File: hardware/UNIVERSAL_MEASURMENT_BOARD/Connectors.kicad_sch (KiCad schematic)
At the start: 17 parts, among them J1 2604-1104, J10 2604-1104, J11 2604-1104, J12 2604-1104, J13 2604-1104, J14 2604-1104, J15 2604-1104, J16 2604-1104, J17 2604-1104, J2 2604-1104, J3 2604-1104, J4 2604-1104, J5 2604-1104, J6 2604-1104, J7 2604-1104, J8 2604-1104, J9 2604-1104

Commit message: continued
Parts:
- removed J11, J12, J16, J3: 2604-1104, 26041104, symbol 2604-1104:2604-1104
- added D1, D10, D11, D12, D13, D14, D15, D16, D17, D18, D19, D2, D20, D21, D22, D23, D24, D25, D26, D27, D28, D29, D3, D30, D31, D32, D33, D34, D35, D36, D37, D38, D39, D4, D40, D5, D6, D7, D8, D9: TVS, symbol Device:D_TVS_Small
- added F1, F10, F11, F12, F14, F15, F16, F17, F18, F19, F2, F20, F21, F22, F23, F24, F25, F26, F27, F28, F29, F3, F30, F31, F32, F33, F34, F35, F36, F37, F4, F5, F6, F7, F8, F9: 100mA, symbol Device:Fuse_Small
- added F13: -A, symbol Device:Fuse_Small
- added unit 3 of J1
- added unit 4 of J1
- added unit 2 of J1
- added unit 2 of J10
- added unit 3 of J10
- added unit 4 of J10
- added J11, J12, J18, J19, J20, J21, J22, J23, J24, J25, J26, J27, J3: 2604-1104, 26041104, symbol 2604-1104:2604-1104
- added unit 4 of J13
- added unit 2 of J13
- added unit 3 of J13
- added unit 3 of J14
- added unit 2 of J14
- added unit 4 of J14
- added unit 4 of J15
- added unit 3 of J15
- added unit 2 of J15
- added J16: PRG, Connector_PinHeader_1.00mm:PinHeader_1x05_P1.00mm_Vertical, symbol Connector:Conn_01x05_Pin
- added unit 3 of J17
- added unit 4 of J17
- added unit 2 of J17
- added unit 4 of J2
- added unit 2 of J2
- added unit 3 of J2
- added unit 4 of J4
- added unit 2 of J4
- added unit 3 of J4
- added unit 4 of J5
- added unit 2 of J5
- added unit 3 of J5
- added unit 3 of J6
- added unit 4 of J6
- added unit 2 of J6
- added unit 4 of J7
- added unit 2 of J7
- added unit 3 of J7
- added unit 4 of J8
- added unit 3 of J8
- added unit 2 of J8
- added unit 4 of J9
- added unit 3 of J9
- added unit 2 of J9
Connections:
- net +12V: now also F1.1, F14.1, F15.1, F16.1, F2.1, F20.1, F21.1, F22.1, F26.1, F27.1, F28.1, F3.1, F32.1, F33.1, F34.1, F7.1, F8.1, F9.1; no longer J2.1 (1.1), J2.2 (1.2), J4.1 (1.1), J4.2 (1.2), J5.1 (1.1), J5.2 (1.2), J6.1 (1.1), J6.2 (1.2), J7.1 (1.1), J7.2 (1.2), J8.1 (1.1), J8.2 (1.2), J9.1 (1.1), J9.2 (1.2)
- net +24V: now also F13.1; no longer J1.1 (1.1), J1.2 (1.2)
- net +5V: now also F10.1, F11.1, F12.1, F17.1, F18.1, F19.1, F23.1, F24.1, F25.1, F29.1, F30.1, F31.1, F35.1, F36.1, F37.1, F4.1, F5.1, F6.1; no longer J10.1 (1.1), J10.2 (1.2), J13.1 (1.1), J13.2 (1.2), J14.1 (1.1), J14.2 (1.2), J15.1 (1.1), J15.2 (1.2), J17.1 (1.1), J17.2 (1.2)
- net A10N: now also D33.2 (A2), J23.3 (2), J23.4 (2.2)
- net A10P: now also D30.2 (A2), J23.1, J23.2 (1.2)
- net A11N: now also D39.2 (A2), J26.5 (3), J26.6 (3.2); no longer J14.5 (3.1), J14.6 (3.2)
- net A11P: now also D36.2 (A2), J26.3 (2), J26.4 (2.2); no longer J14.3 (2.1), J14.4 (2.2)
- net A12N: now also D6.2 (A2), J5.3 (2), J5.4 (2.2)
- net A12P: now also J5.1, J5.2 (1.2), D3.2 (A2)
- net A13N: now also D12.2 (A2), D20.2 (A2), J15.3 (2), J15.4 (2.2), J8.5 (3), J8.6 (3.2)
- net A13P: now also J15.1, J15.2 (1.2), D17.2 (A2), D9.2 (A2), J8.3 (2), J8.4 (2.2)
- net A14N: now also D28.2 (A2), J19.5 (3), J19.6 (3.2); no longer J13.5 (3.1), J13.6 (3.2)
- net A14P: now also D25.2 (A2), J19.3 (2), J19.4 (2.2); no longer J13.3 (2.1), J13.4 (2.2)
- net A15N: now also D34.2 (A2), J24.3 (2), J24.4 (2.2); no longer J15.5 (3.1), J15.6 (3.2)
- net A15P: now also D31.2 (A2), J24.1, J24.2 (1.2); no longer J15.3 (2.1), J15.4 (2.2)
- net A16N: now also D40.2 (A2), J27.5 (3), J27.6 (3.2); no longer J17.5 (3.1), J17.6 (3.2)
- net A16P: now also D37.2 (A2), J27.3 (2), J27.4 (2.2); no longer J17.3 (2.1), J17.4 (2.2)
- net A1N: now also D4.2 (A2), J1.7 (4), J1.8 (4.2); no longer J2.5 (3.1), J2.6 (3.2)
- net A1P: now also D1.2 (A2), J1.5 (3), J1.6 (3.2); no longer J2.3 (2.1), J2.4 (2.2)
- net A2N: now also J9.1, J9.2 (1.2), D10.2 (A2)
- net A2P: now also D7.2 (A2), J6.7 (4), J6.8 (4.2)
- net A3N: now also D18.2 (A2), J13.3 (2), J13.4 (2.2); no longer J4.5 (3.1), J4.6 (3.2)
- net A3P: now also J13.1, J13.2 (1.2), D15.2 (A2); no longer J4.3 (2.1), J4.4 (2.2)
- net A4N: now also D26.2 (A2), J17.5 (3), J17.6 (3.2); no longer J5.5 (3.1), J5.6 (3.2)
- net A4P: now also D23.2 (A2), J17.3 (2), J17.4 (2.2); no longer J5.3 (2.1), J5.4 (2.2)
- net A5N: now also D32.2 (A2), J20.7 (4), J20.8 (4.2); no longer J6.5 (3.1), J6.6 (3.2)
- net A5P: now also D29.2 (A2), J20.5 (3), J20.6 (3.2); no longer J6.3 (2.1), J6.4 (2.2)
- net A6N: now also J2.1, J2.2 (1.2), D38.2 (A2); no longer J7.5 (3.1), J7.6 (3.2)
- net A6P: now also D35.2 (A2), J25.7 (4), J25.8 (4.2); no longer J7.3 (2.1), J7.4 (2.2)
- net A7N: now also D5.2 (A2), J4.3 (2), J4.4 (2.2); no longer J8.5 (3.1), J8.6 (3.2)
- net A7P: now also J4.1, J4.2 (1.2), D2.2 (A2); no longer J8.3 (2.1), J8.4 (2.2)
- net A8N: now also D11.2 (A2), J7.5 (3), J7.6 (3.2); no longer J9.5 (3.1), J9.6 (3.2)
- net A8P: now also D8.2 (A2), J7.3 (2), J7.4 (2.2); no longer J9.3 (2.1), J9.4 (2.2)
- net A9N: now also D19.2 (A2), D27.2 (A2), J14.3 (2), J14.4 (2.2), J18.5 (3), J18.6 (3.2); no longer J10.5 (3.1), J10.6 (3.2)
- net A9P: now also J14.1, J14.2 (1.2), D16.2 (A2), D24.2 (A2), J18.3 (2), J18.4 (2.2); no longer J10.3 (2.1), J10.4 (2.2)
- net CANH: now also D13.2 (A2), J10.5 (3), J10.6 (3.2); no longer J1.3 (2.1), J1.4 (2.2)
- net CANL: now also D14.2 (A2), J10.7 (4), J10.8 (4.2); no longer J1.5 (3.1), J1.6 (3.2)
- net GND: now also J6.1, J6.2 (1.2), D1.1 (A1), D10.1 (A1), D11.1 (A1), D12.1 (A1), D15.1 (A1), D16.1 (A1), D17.1 (A1), D18.1 (A1), D19.1 (A1), D2.1 (A1), D20.1 (A1), D21.1 (A1), D22.1 (A1), D23.1 (A1), D24.1 (A1), D25.1 (A1), D26.1 (A1), D27.1 (A1), D28.1 (A1), D29.1 (A1), D3.1 (A1), D30.1 (A1), D31.1 (A1), D32.1 (A1), D33.1 (A1), D34.1 (A1), D35.1 (A1), D36.1 (A1), D37.1 (A1), D38.1 (A1), D39.1 (A1), D4.1 (A1), D40.1 (A1), D5.1 (A1), D6.1 (A1), D7.1 (A1), D8.1 (A1), D9.1 (A1), J10.3 (2), J10.4 (2.2), J13.5 (3), J13.6 (3.2), J14.5 (3), J14.6 (3.2), J15.5 (3), J15.6 (3.2), J16.1 (Pin_1), J17.7 (4), J17.8 (4.2), J18.7 (4), J18.8 (4.2), J19.7 (4), J19.8 (4.2), J2.3 (2), J2.4 (2.2), J23.5 (3), J23.6 (3.2), J24.5 (3), J24.6 (3.2), J25.1, J25.2 (1.2), J26.7 (4), J26.8 (4.2), J27.7 (4), J27.8 (4.2), J4.5 (3), J4.6 (3.2), J5.5 (3), J5.6 (3.2), J7.7 (4), J7.8 (4.2), J8.7 (4), J8.8 (4.2), J9.3 (2), J9.4 (2.2); no longer J1.7 (4.1), J1.8 (4.2), J10.7 (4.1), J10.8 (4.2), J13.7 (4.1), J13.8 (4.2), J14.7 (4.1), J14.8 (4.2), J15.7 (4.1), J15.8 (4.2), J17.7 (4.1), J17.8 (4.2), J2.7 (4.1), J2.8 (4.2), J4.7 (4.1), J4.8 (4.2), J5.7 (4.1), J5.8 (4.2), J6.7 (4.1), J6.8 (4.2), J7.7 (4.1), J7.8 (4.2), J8.7 (4.1), J8.8 (4.2), J9.7 (4.1), J9.8 (4.2)
- new net: F28.2, J22.5 (3), J22.6 (3.2)
- new net: F13.2, J10.1, J10.2 (1.2)
- new net: F19.2, J12.7 (4), J12.8 (4.2)
- new net: F9.2, J5.7 (4), J5.8 (4.2)
- new net: F11.2, J7.1, J7.2 (1.2)
- new net: F12.2, J8.1, J8.2 (1.2)
- new net: F30.2, J21.7 (4), J21.8 (4.2)
- new net: F24.2, J18.1, J18.2 (1.2)
- new net: F35.2, J25.5 (3), J25.6 (3.2)
- new net: F10.2, J6.5 (3), J6.6 (3.2)
- new net: F1.2, J1.1, J1.2 (1.2)
- new net: F8.2, J4.7 (4), J4.8 (4.2)
- new net: F22.2, J15.7 (4), J15.8 (4.2)
- new net: F20.2, J13.7 (4), J13.8 (4.2)
- new net: F5.2, J2.7 (4), J2.8 (4.2)
- new net: F32.2, J25.3 (2), J25.4 (2.2)
- new net: F3.2, J3.5 (3), J3.6 (3.2)
- new net: F31.2, J22.7 (4), J22.8 (4.2)
- new net: F25.2, J19.1, J19.2 (1.2)
- new net: F15.2, J11.5 (3), J11.6 (3.2)
- new net: F26.2, J20.1, J20.2 (1.2)
- new net: F33.2, J23.7 (4), J23.8 (4.2)
- new net: F36.2, J26.1, J26.2 (1.2)
- new net: F4.2, J1.3 (2), J1.4 (2.2)
- new net: F37.2, J27.1, J27.2 (1.2)
- new net: F27.2, J21.5 (3), J21.6 (3.2)
- new net: F23.2, J17.1, J17.2 (1.2)
- new net: F2.2, J2.5 (3), J2.6 (3.2)
- new net: F17.2, J9.7 (4), J9.8 (4.2)
- new net: F29.2, J20.3 (2), J20.4 (2.2)
- new net: F34.2, J24.7 (4), J24.8 (4.2)
- new net: F14.2, J9.5 (3), J9.6 (3.2)
- new net: F7.2, J6.3 (2), J6.4 (2.2)
- new net: F16.2, J12.5 (3), J12.6 (3.2)
- new net: F21.2, J14.7 (4), J14.8 (4.2)
- new net: F6.2, J3.7 (4), J3.8 (4.2)
- new net: F18.2, J11.7 (4), J11.8 (4.2)
- new net +3V3: J16.5 (Pin_5)
- new net GND_ISO: D13.1 (A1), D14.1 (A1)
- new net RST: J16.2 (Pin_2)
- new net SWCLK: D21.2 (A2), J16.4 (Pin_4)
- new net SWDIO: D22.2 (A2), J16.3 (Pin_3)
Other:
- note added: "CHN1"
- note added: "CHN10"
- note added: "CHN11"
- note added: "CHN12"
- note added: "CHN13"
- note added: "CHN14"
- note added: "CHN15"
- note added: "CHN16"
- note added: "CHN2"
- note added: "CHN3"
- note added: "CHN4"
- note added: "CHN5"
- note added: "CHN6"
- note added: "CHN7"
- note added: "CHN8"
- note added: "CHN9"
- note added: "MCU SWD PORT"
- note added: "Measure Channels Connectors"
- note added: "POWER & CAN PORT"
- note added: "Programming Port"
- note added: "Supply and CAN Connector"
- note removed: "12V CHN"
- note removed: "5V CHN"
- note removed: "POWER / CAN"
- company: (none) -> PUT Motorsport Formula Student team
- title: (none) -> Universal Measurment Board

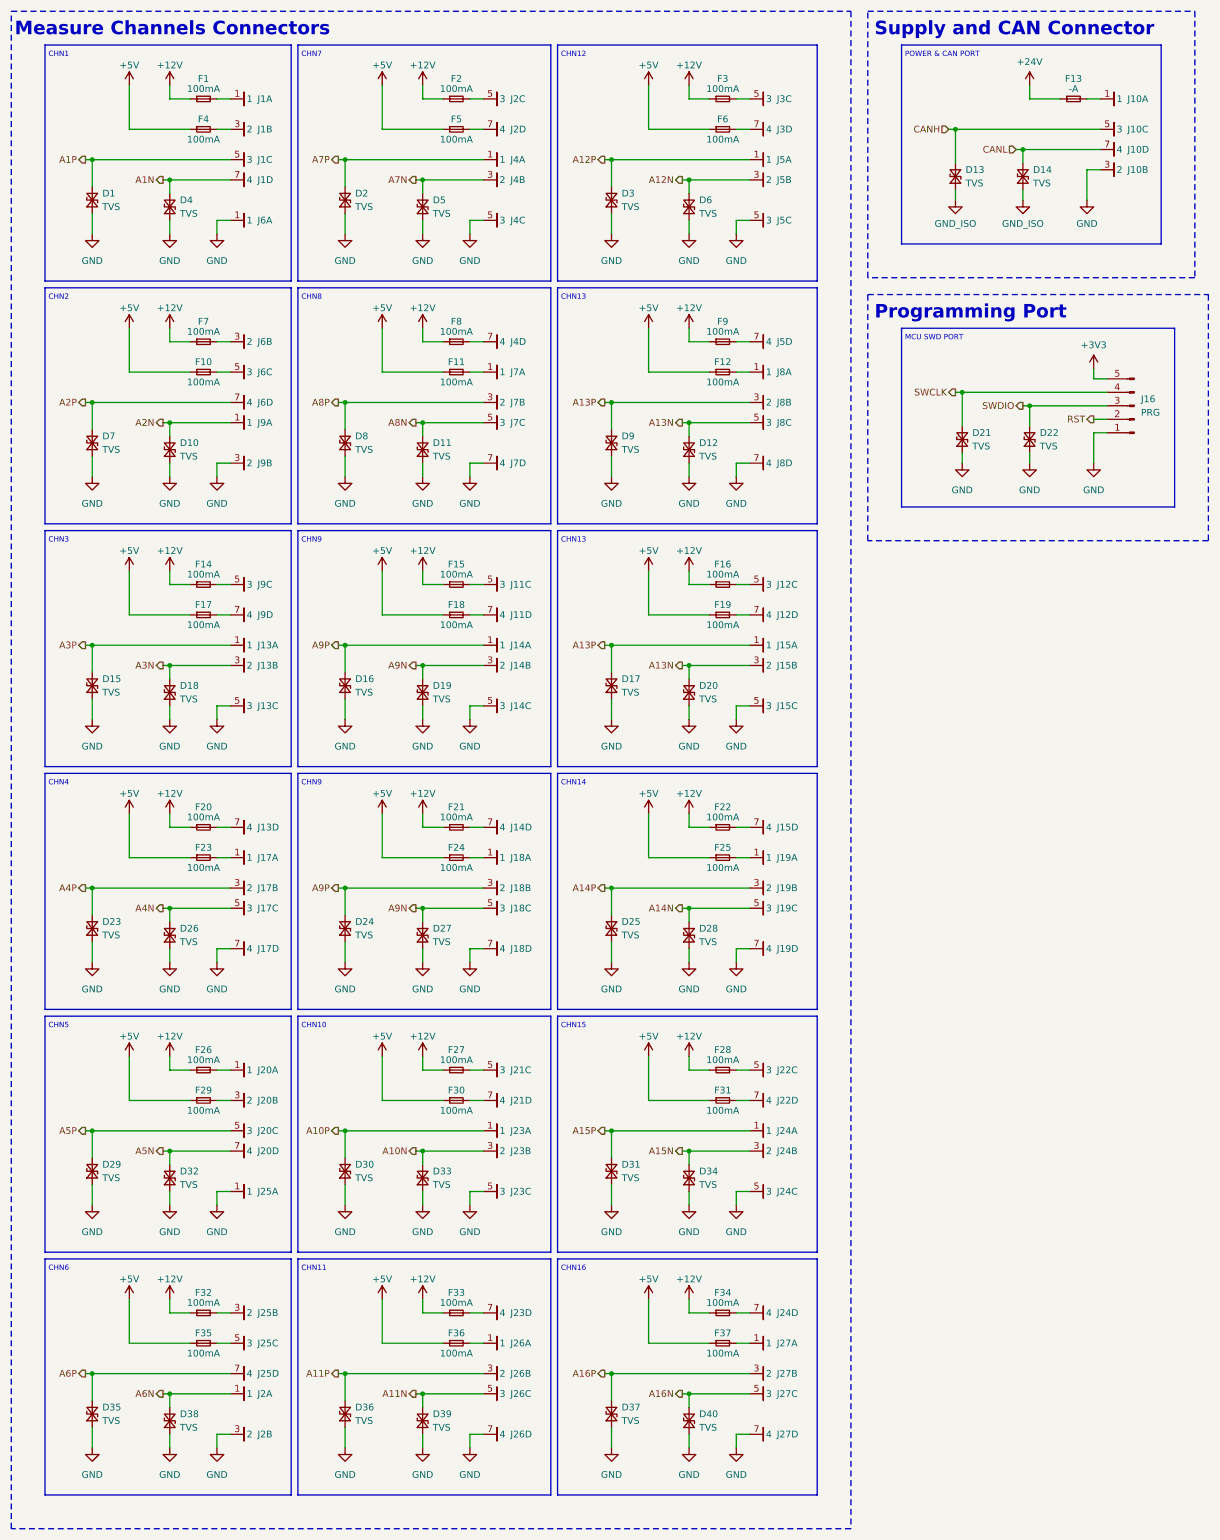
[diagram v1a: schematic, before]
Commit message: schematic review corrections
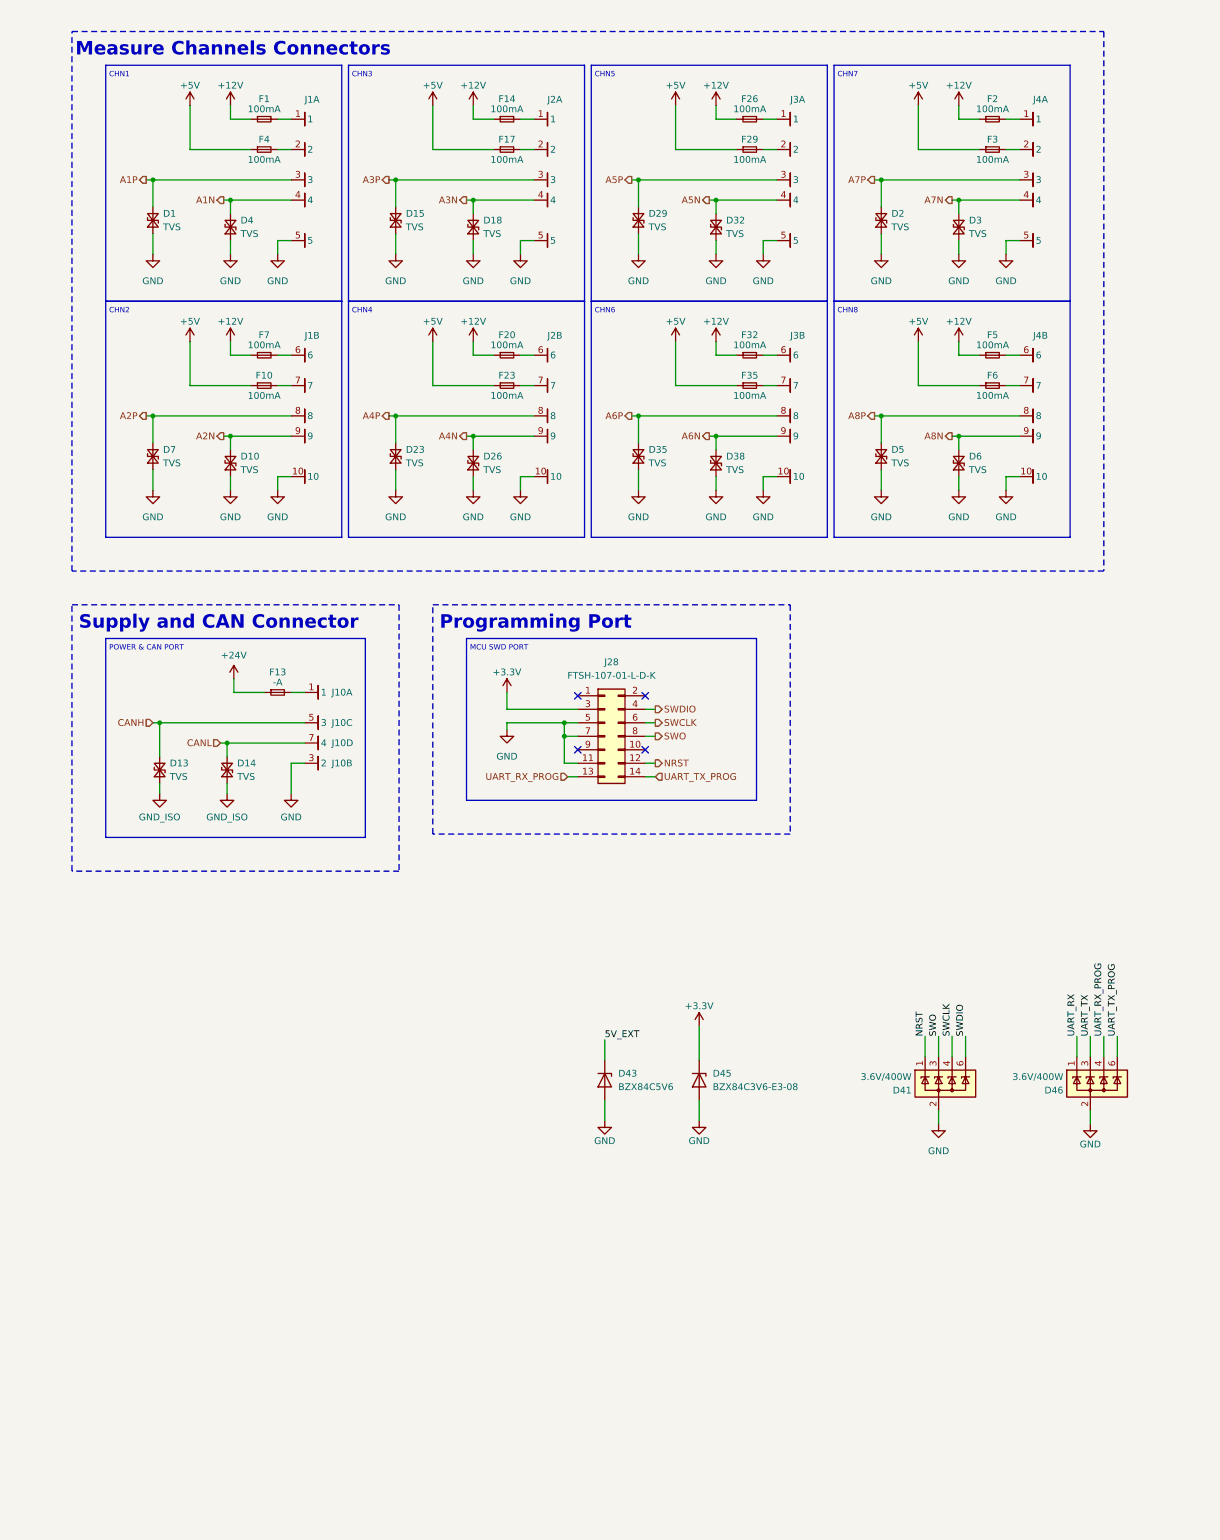
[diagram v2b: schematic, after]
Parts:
- removed D11, D12, D16, D17, D19, D20, D21, D22, D24, D25, D27, D28, D30, D31, D33, D34, D36, D37, D39, D40, D8, D9: TVS, symbol Device:D_TVS_Small
- removed F11, F12, F15, F16, F18, F19, F21, F22, F24, F25, F27, F28, F30, F31, F33, F34, F36, F37, F8, F9: 100mA, symbol Device:Fuse_Small
- removed J1, J11, J12, J13, J14, J15, J17, J18, J19, J2, J20, J21, J22, J23, J24, J25, J26, J27, J3, J4, J5, J6, J7, J8, J9: 2604-1104, 26041104, symbol 2604-1104:2604-1104
- removed J16: PRG, Connector_PinHeader_1.00mm:PinHeader_1x05_P1.00mm_Vertical, symbol Connector:Conn_01x05_Pin
- added D41, D46: 3.6V/400W, Package_TO_SOT_SMD:SOT-23-6, symbol Power_Protection:ESDA5V3SC5
- added D43: BZX84C5V6, Package_TO_SOT_SMD:SOT-23, symbol Diode:BZX84Cxx
- added D45: BZX84C3V6-E3-08, Package_TO_SOT_SMD:SOT-23, symbol Diode:BZX84Cxx
- added J1, J3, J4: 2606-1110_010-000, 26061110010000, symbol 2604-1110:2606-1110_010-000
- added J2: 2606-1110_010-000, 2604-1110:26041110, symbol 2604-1110:2606-1110_010-000
- added J28: FTSH-107-01-L-D-K, Samacsys:FTSH-107-XX-YYY-D-K, symbol Samacsys_kicad_sym:FTSH-107-01-L-D-K
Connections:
- net A12N is gone; now on net A8N: D6.2 (A2)
- net A12P is gone; now on net A7N: D3.2 (A2)
- net +12V: now also F5.1; no longer F3.1
- net +5V: now also F3.1; no longer F5.1
- net A1N: now also J1.4
- net A1P: now also J1.3
- net A2N: now also J1.9
- net A2P: now also J1.8
- net A3N: now also J2.4
- net A3P: now also J2.3
- net A4N: now also J2.9
- net A4P: now also J2.8
- net A5N: now also J3.4
- net A5P: now also J3.3
- net A6N: now also J3.9
- net A6P: now also J3.8
- net A7N: now also J4.4; no longer D5.2 (A2)
- net A7P: now also J4.3
- net A8N: now also J4.9
- net A8P: now also D5.2 (A2), J4.8
- net GND: now also D41.2 (K), D41.5 (NC), D43.1 (A), D45.1 (A), D46.2 (K), D46.5 (NC), J1.10, J1.5, J2.10, J2.5, J28.11 (Pin_11), J28.5 (Pin_5), J28.7 (Pin_7), J3.10, J3.5, J4.10, J4.5
- net SWCLK: now also D41.4 (A), J28.6 (Pin_6)
- net SWDIO: now also D41.6 (A), J28.4 (Pin_4)
- net at F35.2: now also J3.7
- net at F10.2: now also J1.7
- net at F1.2: now also J1.1
- net at F20.2: now also J2.6
- net at F5.2: now also J4.6
- net at F32.2: now also J3.6
- net at F3.2: now also J4.2
- net at F26.2: now also J3.1
- net at F4.2: now also J1.2
- net at F23.2: now also J2.7
- net at F2.2: now also J4.1
- net at F17.2: now also J2.2
- net at F29.2: now also J3.2
- net at F14.2: now also J2.1
- net at F7.2: now also J1.6
- net at F6.2: now also J4.7
- new net +3.3V: D45.3 (K), J28.3 (Pin_3)
- new net 5V_EXT: D43.3 (K)
- new net NRST: D41.1 (A), J28.12 (Pin_12)
- new net SWO: D41.3 (A), J28.8 (Pin_8)
- new net UART_RX: D46.1 (A)
- new net UART_RX_PROG: D46.4 (A), J28.13 (Pin_13)
- new net UART_TX: D46.3 (A)
- new net UART_TX_PROG: D46.6 (A), J28.14 (Pin_14)
- no-connect marks 0 -> 4
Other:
- note removed: "CHN10"
- note removed: "CHN11"
- note removed: "CHN12"
- note removed: "CHN13"
- note removed: "CHN14"
- note removed: "CHN15"
- note removed: "CHN16"
- note removed: "CHN9"
- moved on the sheet: D1, D10, D13, D14, D15, D18, D23, D26, D29, D32, D35, D38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

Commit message: final schematic review corrections
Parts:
- removed D41, D46: 3.6V/400W, Package_TO_SOT_SMD:SOT-23-6, symbol Power_Protection:ESDA5V3SC5
- removed D43: BZX84C5V6, Package_TO_SOT_SMD:SOT-23, symbol Diode:BZX84Cxx
- removed D45: BZX84C3V6-E3-08, Package_TO_SOT_SMD:SOT-23, symbol Diode:BZX84Cxx
- removed J10: 2604-1104, 26041104, symbol 2604-1104:2604-1104
- added J5: 2604-1104, 2601-1104:26011104, symbol 2601-1104:2604-1104
- added U17, U18: ESDS304DBVR, SOT95P280X145-5N, symbol ESDS304DBVR:ESDS304DBVR
- J1, J3, J4: footprint 26061110010000 -> 2601-1110:26011110
- J2: footprint 2604-1110:26041110 -> 2601-1110:26011110
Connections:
- net +3.3V: now also U18.1; no longer J28.3 (Pin_3)
- net CANH: now also J5.5 (3), J5.6 (3.2)
- net CANL: now also J5.7 (4), J5.8 (4.2)
- net GND: now also J5.3 (2), J5.4 (2.2), U17.2, U17.2, U17.2, U17.2, U18.2, U18.2, U18.2, U18.2
- net NRST: now also U17.1
- net SWCLK: now also U17.4
- net SWDIO: now also U17.5
- net SWO: now also U17.3
- net UART_RX_PROG: now also U18.5
- net UART_TX_PROG: now also U18.4
- net at F13.2: now also J5.1, J5.2 (1.2)
- net +12V renamed +12V0
- net +24V renamed +24V0
- net +5V renamed +5V0
- new net +3V3: J28.3 (Pin_3)
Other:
- moved on the sheet: D13, D14, F13, J28
